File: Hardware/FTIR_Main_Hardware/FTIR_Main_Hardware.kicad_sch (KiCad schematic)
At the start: 63 parts, among them J1 RJ45_LED_Shielded, Q1 IRF7606PBF, Q2 BSS138, Q3 IRF7606PBF, Q4 IRF7606PBF, Q5 BSS138, Q6 BSS138, U1 Opamp_Dual, U2 D36V28F7, U3 OKI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

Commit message: Laser Diode Footprint
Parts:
- LD1: footprint (none) -> MRDT_Actives:DIO_PL_450B
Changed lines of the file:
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@@
       (effects (font (size 1.27 1.27)) (justify left))
     )
-    (property "Footprint" "" (at 205.105 171.45 0)
+    (property "Footprint" "MRDT_Actives:DIO_PL_450B" (at 205.105 171.45 0)
       (effects (font (size 1.27 1.27)) hide)
     )

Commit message: Footprints for LD and Stepper Driver fr this time
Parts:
- LD1: footprint MRDT_Actives:DIO_PL_450B -> Pakcage:DIO_PL_450B
- U1: footprint Package_SO:SO-8_3.9x4.9mm_P1.27mm -> (none)
- U2: footprint MRDT_Devices:D36V28F7_Buck -> (none)
- U4: footprint MRDT_Shields:MODULE_TMC2208_SILENTSTEPSTICK -> Pakcage:MODULE_TMC2208_SILENTSTEPSTICK
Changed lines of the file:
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@@
       (effects (font (size 1.27 1.27)))
     )
-    (property "Footprint" "Package_SO:SO-8_3.9x4.9mm_P1.27mm" (at 40.005 180.975 0)
+    (property "Footprint" "" (at 40.005 180.975 0)
       (effects (font (size 1.27 1.27)) hide)
     )
@@
       (effects (font (size 1.27 1.27)))
     )
-    (property "Footprint" "MRDT_Devices:D36V28F7_Buck" (at 40.64 75.565 0)
+    (property "Footprint" "" (at 40.64 75.565 0)
       (effects (font (size 1.27 1.27)) hide)
     )
@@
       (effects (font (size 1.27 1.27)))
     )
-    (property "Footprint" "MRDT_Shields:MODULE_TMC2208_SILENTSTEPSTICK" (at 87.63 115.57 0)
+    (property "Footprint" "Pakcage:MODULE_TMC2208_SILENTSTEPSTICK" (at 87.63 115.57 0)
       (effects (font (size 1.27 1.27)) hide)
     )
@@
       (effects (font (size 1.27 1.27)))
     )
-    (property "Footprint" "Package_SO:SO-8_3.9x4.9mm_P1.27mm" (at 102.235 181.61 0)
+    (property "Footprint" "" (at 102.235 181.61 0)
       (effects (font (size 1.27 1.27)) hide)
     )
@@
       (effects (font (size 1.27 1.27)))
     )
-    (property "Footprint" "Package_SO:SO-8_3.9x4.9mm_P1.27mm" (at 72.39 153.67 0)
+    (property "Footprint" "" (at 72.39 153.67 0)
       (effects (font (size 1.27 1.27)) hide)
     )
@@
       (effects (font (size 1.27 1.27)) (justify left))
     )
-    (property "Footprint" "MRDT_Actives:DIO_PL_450B" (at 205.105 171.45 0)
-      (effects (font (size 1.27 1.27)) hide)
-    )
+    (property "Footprint" "Pakcage:DIO_PL_450B" (at 205.105 171.45 0)
+      (effects (font (size 1.27 1.27)) hide)
+    )

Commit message: Fixed footprints??????
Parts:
- LD1: footprint Pakcage:DIO_PL_450B -> FTIR_Footprints:DIO_PL_450B
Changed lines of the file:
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@@
       (effects (font (size 1.27 1.27)) (justify left))
     )
-    (property "Footprint" "Pakcage:DIO_PL_450B" (at 205.105 171.45 0)
+    (property "Footprint" "FTIR_Footprints:DIO_PL_450B" (at 205.105 171.45 0)
       (effects (font (size 1.27 1.27)) hide)
     )

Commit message: Checked Footprints
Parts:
- U4: footprint Pakcage:MODULE_TMC2208_SILENTSTEPSTICK -> FTIR_Footprints:MODULE_TMC2208_SILENTSTEPSTICK
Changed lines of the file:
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@@
       (effects (font (size 1.27 1.27)))
     )
-    (property "Footprint" "Pakcage:MODULE_TMC2208_SILENTSTEPSTICK" (at 87.63 115.57 0)
+    (property "Footprint" "FTIR_Footprints:MODULE_TMC2208_SILENTSTEPSTICK" (at 87.63 115.57 0)
       (effects (font (size 1.27 1.27)) hide)
     )

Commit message: Finished Footprints (!)
I want to sleep :(
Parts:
- Conn10, Conn3, Conn5, Conn9: footprint (none) -> MRDT_Connectors:142-0701-801
- D1: footprint (none) -> MRDT_Sensors:P16113-011MN
- D3: footprint (none) -> MRDT_Sensors:VTP9812FH
- LD1: footprint FTIR_Footprints:DIO_PL_450B -> FTIR_Footprints:RLD63NPC5
- U1: footprint (none) -> Package_SO:SO-8_3.9x4.9mm_P1.27mm
- U2: footprint (none) -> MRDT_Devices:D36V28F7_Buck
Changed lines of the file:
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@@
       (effects (font (size 1.27 1.27)))
     )
-    (property "Footprint" "" (at 40.005 180.975 0)
+    (property "Footprint" "Package_SO:SO-8_3.9x4.9mm_P1.27mm" (at 40.005 180.975 0)
       (effects (font (size 1.27 1.27)) hide)
     )
@@
       (effects (font (size 1.27 1.27)))
     )
-    (property "Footprint" "" (at 40.64 75.565 0)
+    (property "Footprint" "MRDT_Devices:D36V28F7_Buck" (at 40.64 75.565 0)
       (effects (font (size 1.27 1.27)) hide)
     )
@@
       (effects (font (size 1.27 1.27)))
     )
-    (property "Footprint" "" (at 102.235 181.61 0)
+    (property "Footprint" "Package_SO:SO-8_3.9x4.9mm_P1.27mm" (at 102.235 181.61 0)
       (effects (font (size 1.27 1.27)) hide)
     )
@@
       (effects (font (size 1.27 1.27)) (justify left))
     )
-    (property "Footprint" "" (at 86.995 184.785 0)
+    (property "Footprint" "MRDT_Sensors:VTP9812FH" (at 86.995 184.785 0)
       (effects (font (size 1.27 1.27)) hide)
     )
@@
       (effects (font (size 1.27 1.27)))
     )
-    (property "Footprint" "" (at 72.39 153.67 0)
+    (property "Footprint" "Package_SO:SO-8_3.9x4.9mm_P1.27mm" (at 72.39 153.67 0)
       (effects (font (size 1.27 1.27)) hide)
     )
@@
       (effects (font (size 1.27 1.27)) (justify left))
     )
-    (property "Footprint" "FTIR_Footprints:DIO_PL_450B" (at 205.105 171.45 0)
+    (property "Footprint" "FTIR_Footprints:RLD63NPC5" (at 205.105 171.45 0)
       (effects (font (size 1.27 1.27)) hide)
     )
@@
       (effects (font (size 1.524 1.524)) (justify right))
     )
-    (property "Footprint" "" (at 65.405 180.975 0)
+    (property "Footprint" "MRDT_Connectors:142-0701-801" (at 65.405 180.975 0)
       (effects (font (size 1.524 1.524)) hide)
     )
@@
       (effects (font (size 1.27 1.27)) (justify left))
     )
-    (property "Footprint" "" (at 24.765 184.15 0)
+    (property "Footprint" "MRDT_Sensors:P16113-011MN" (at 24.765 184.15 0)
       (effects (font (size 1.27 1.27)) hide)
     )
@@
       (effects (font (size 1.524 1.524)) (justify right))
     )
-    (property "Footprint" "" (at 126.365 181.61 0)
+    (property "Footprint" "MRDT_Connectors:142-0701-801" (at 126.365 181.61 0)
       (effects (font (size 1.524 1.524)) hide)
     )
@@
       (effects (font (size 1.524 1.524)) (justify right))
     )
-    (property "Footprint" "" (at 202.565 112.395 0)
+    (property "Footprint" "MRDT_Connectors:142-0701-801" (at 202.565 112.395 0)
       (effects (font (size 1.524 1.524)) hide)
     )
@@
       (effects (font (size 1.524 1.524)) (justify right))
     )
-    (property "Footprint" "" (at 266.065 112.395 0)
-      (effects (font (size 1.524 1.524)) hide)
-    )
+    (property "Footprint" "MRDT_Connectors:142-0701-801" (at 266.065 112.395 0)
+      (effects (font (size 1.524 1.524)) hide)
+    )

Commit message: Moved footprints to local folder
Should work now?
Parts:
- Conn10, Conn3, Conn5, Conn9: footprint MRDT_Connectors:142-0701-801 -> FTIR_Footprints:142-0701-801
- D1: footprint MRDT_Sensors:P16113-011MN -> FTIR_Footprints:P16113-011MN
- D3: footprint MRDT_Sensors:VTP9812FH -> FTIR_Footprints:VTP9812FH
- U2: footprint MRDT_Devices:D36V28F7_Buck -> FTIR_Footprints:D36V28F7_Buck
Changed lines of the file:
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@@
       (effects (font (size 1.27 1.27)))
     )
-    (property "Footprint" "MRDT_Devices:D36V28F7_Buck" (at 40.64 75.565 0)
+    (property "Footprint" "FTIR_Footprints:D36V28F7_Buck" (at 40.64 75.565 0)
       (effects (font (size 1.27 1.27)) hide)
     )
@@
       (effects (font (size 1.27 1.27)) (justify left))
     )
-    (property "Footprint" "MRDT_Sensors:VTP9812FH" (at 86.995 184.785 0)
+    (property "Footprint" "FTIR_Footprints:VTP9812FH" (at 86.995 184.785 0)
       (effects (font (size 1.27 1.27)) hide)
     )
@@
       (effects (font (size 1.524 1.524)) (justify right))
     )
-    (property "Footprint" "MRDT_Connectors:142-0701-801" (at 65.405 180.975 0)
+    (property "Footprint" "FTIR_Footprints:142-0701-801" (at 65.405 180.975 0)
       (effects (font (size 1.524 1.524)) hide)
     )
@@
       (effects (font (size 1.27 1.27)) (justify left))
     )
-    (property "Footprint" "MRDT_Sensors:P16113-011MN" (at 24.765 184.15 0)
+    (property "Footprint" "FTIR_Footprints:P16113-011MN" (at 24.765 184.15 0)
       (effects (font (size 1.27 1.27)) hide)
     )
@@
       (effects (font (size 1.524 1.524)) (justify right))
     )
-    (property "Footprint" "MRDT_Connectors:142-0701-801" (at 126.365 181.61 0)
+    (property "Footprint" "FTIR_Footprints:142-0701-801" (at 126.365 181.61 0)
       (effects (font (size 1.524 1.524)) hide)
     )
@@
       (effects (font (size 1.524 1.524)) (justify right))
     )
-    (property "Footprint" "MRDT_Connectors:142-0701-801" (at 202.565 112.395 0)
+    (property "Footprint" "FTIR_Footprints:142-0701-801" (at 202.565 112.395 0)
       (effects (font (size 1.524 1.524)) hide)
     )
@@
       (effects (font (size 1.524 1.524)) (justify right))
     )
-    (property "Footprint" "MRDT_Connectors:142-0701-801" (at 266.065 112.395 0)
-      (effects (font (size 1.524 1.524)) hide)
-    )
+    (property "Footprint" "FTIR_Footprints:142-0701-801" (at 266.065 112.395 0)
+      (effects (font (size 1.524 1.524)) hide)
+    )

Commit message: Began Layout
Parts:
- removed D1: D_Photo, FTIR_Footprints:P16113-011MN, symbol Device:D_Photo
- removed D3: D_Photo, FTIR_Footprints:VTP9812FH, symbol Device:D_Photo
- added D1: D_Photo, FTIR_Footprints:VTP9812FH, symbol Sensor_Optical:S5971
- added D11: S5971, FTIR_Footprints:P16113-011MN, symbol Sensor_Optical:S5971
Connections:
- net GND: now also D1.3 (A), D11.3 (A)
- net at R1.1, U1.2 (-): now also D11.1 (K)
- net at R5.1, U1.6 (-): now also D1.1 (K)

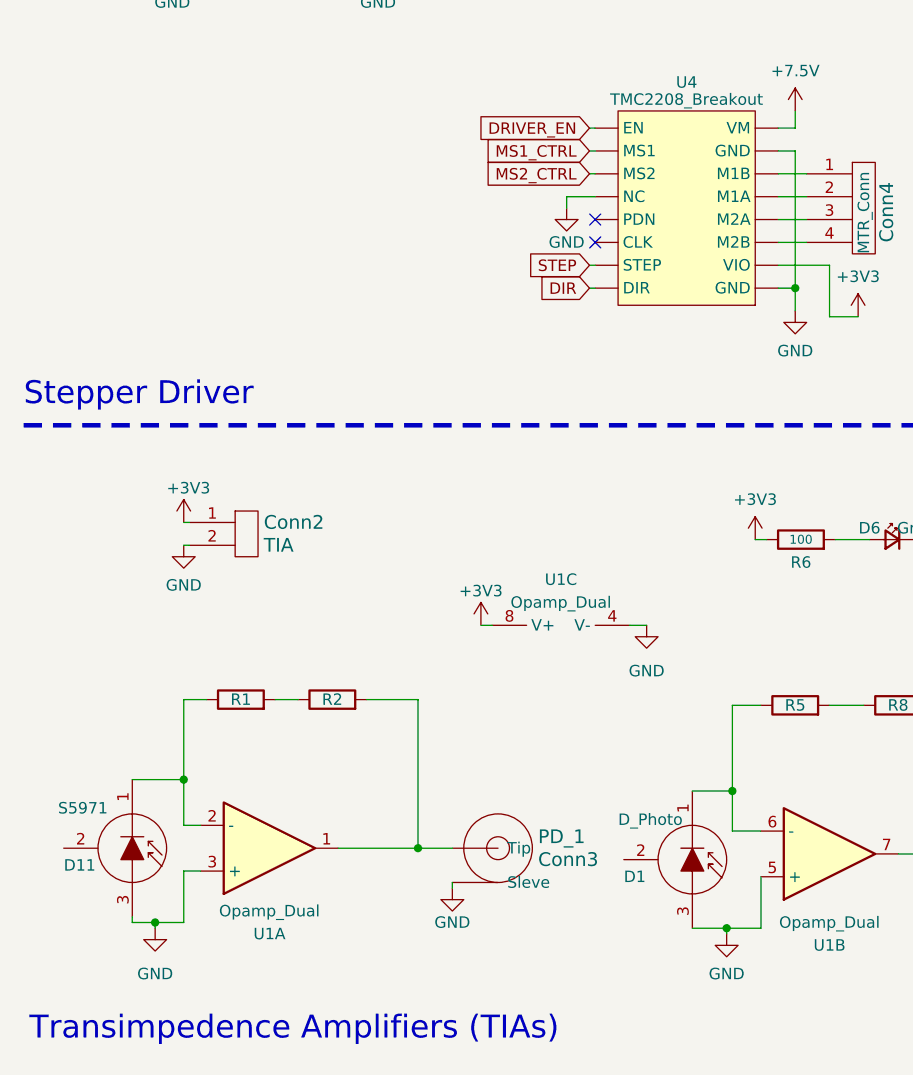
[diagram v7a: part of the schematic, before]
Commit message: updating footprint libraries
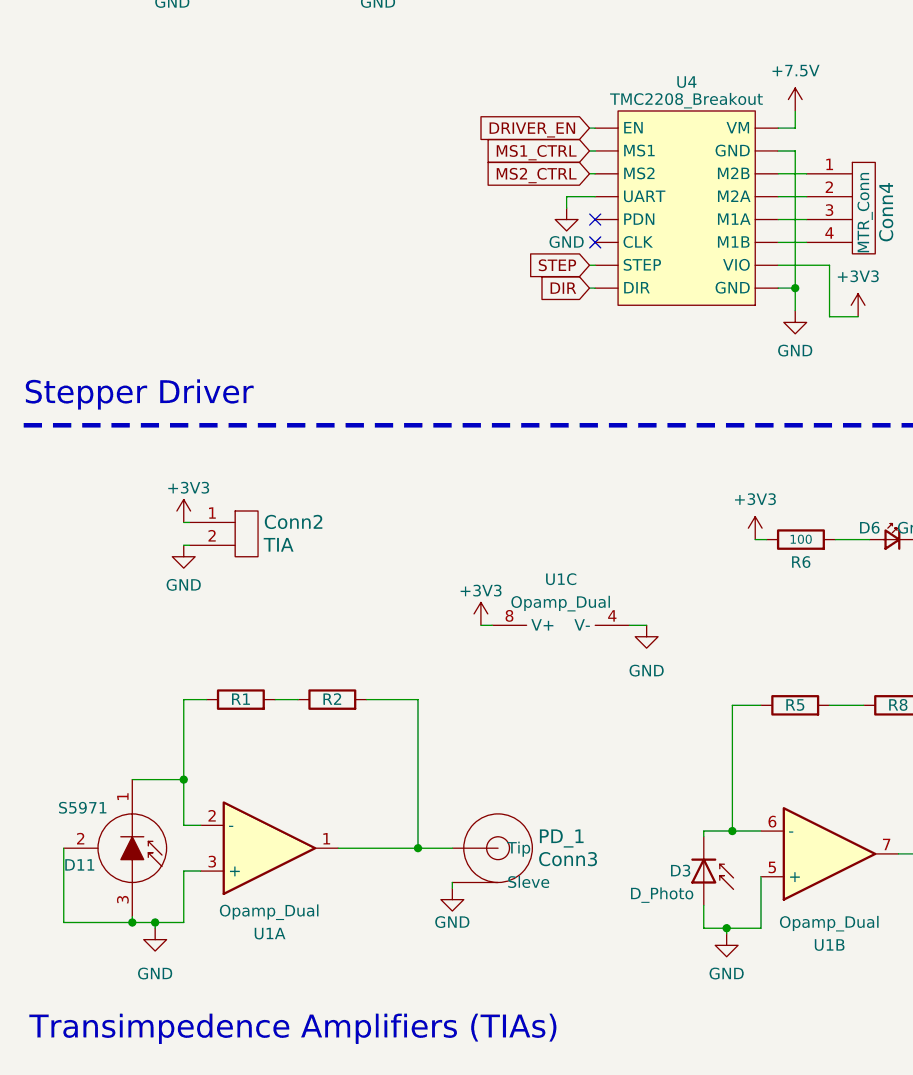
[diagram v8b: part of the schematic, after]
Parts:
- removed D1: D_Photo, FTIR_Footprints:VTP9812FH, symbol Sensor_Optical:S5971
- added D3: D_Photo, FTIR_Footprints:VTP9812FH, symbol Device:D_Photo
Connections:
- net GND: now also D11.2 (C), D3.2 (A)
- net at R5.1, U1.6 (-): now also D3.1 (K)
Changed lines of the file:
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@@
     (company "Mars Rover Design Team")
   )
-  (junction (at 90.805 189.865) (diameter 0) (color 0 0 0 0)
-  )
   (junction (at 305.435 26.67) (diameter 0) (color 0 0 0 0)
   )
@@
   (junction (at 156.845 117.475) (diameter 0) (color 0 0 0 0)
   )
+  (junction (at 91.44 179.07) (diameter 0) (color 0 0 0 0)
+  )
   (junction (at 27.305 189.23) (diameter 0) (color 0 0 0 0)
   )
   (junction (at 30.48 173.355) (diameter 0) (color 0 0 0 0)
   )
-  (junction (at 91.44 174.625) (diameter 0) (color 0 0 0 0)
-  )
   (junction (at 45.72 38.735) (diameter 0) (color 0 0 0 0)
   )
@@
   (junction (at 297.18 38.1) (diameter 0) (color 0 0 0 0)
   )
+  (junction (at 90.805 189.865) (diameter 0) (color 0 0 0 0)
+  )
   (junction (at 117.475 181.61) (diameter 0) (color 0 0 0 0)
   )
@@
   (junction (at 133.985 52.705) (diameter 0) (color 0 0 0 0)
   )
+  (junction (at 24.765 189.23) (diameter 0) (color 0 0 0 0)
+  )
   (junction (at 98.425 118.745) (diameter 0) (color 0 0 0 0)
   )
@@
     (stroke (width 0) (type default))
   )
+  (wire (pts (xy 91.44 179.07) (xy 94.615 179.07))
+    (stroke (width 0) (type default))
+  )
   (wire (pts (xy 56.515 180.975) (xy 60.325 180.975))
     (stroke (width 0) (type default))
@@
     (stroke (width 0) (type default))
   )
-  (wire (pts (xy 91.44 174.625) (xy 91.44 179.07))
-    (stroke (width 0) (type default))
-  )
   (wire (pts (xy 90.805 189.865) (xy 94.615 189.865))
     (stroke (width 0) (type default))
@@
     (stroke (width 0) (type default))
   )
-  (wire (pts (xy 86.995 189.865) (xy 90.805 189.865))
-    (stroke (width 0) (type default))
-  )
   (wire (pts (xy 300.355 113.03) (xy 300.355 111.76))
     (stroke (width 0) (type default))
@@
     (stroke (width 0) (type default))
   )
+  (wire (pts (xy 91.44 165.1) (xy 91.44 179.07))
+    (stroke (width 0) (type default))
+  )
   (wire (pts (xy 297.18 38.1) (xy 300.355 38.1))
     (stroke (width 0) (type default))
@@
     (stroke (width 0.508) (type dash_dot_dot))
   )
+  (wire (pts (xy 88.265 179.705) (xy 88.265 179.07))
+    (stroke (width 0) (type default))
+  )
   (wire (pts (xy 69.85 28.575) (xy 73.66 28.575))
     (stroke (width 0) (type default))
@@
     (stroke (width 0) (type dash))
   )
-  (wire (pts (xy 91.44 179.07) (xy 94.615 179.07))
+  (wire (pts (xy 88.265 179.07) (xy 91.44 179.07))
     (stroke (width 0) (type default))
   )
@@
     (stroke (width 0) (type default))
   )
-  (wire (pts (xy 91.44 165.1) (xy 91.44 174.625))
-    (stroke (width 0) (type default))
-  )
   (wire (pts (xy 178.435 154.305) (xy 180.34 154.305))
     (stroke (width 0) (type default))
@@
     (stroke (width 0) (type default))
   )
-  (wire (pts (xy 86.995 174.625) (xy 91.44 174.625))
-    (stroke (width 0) (type default))
-  )
   (wire (pts (xy 154.305 45.085) (xy 154.305 44.45))
     (stroke (width 0) (type default))
@@
     (stroke (width 0) (type default))
   )
+  (wire (pts (xy 17.145 189.23) (xy 24.765 189.23))
+    (stroke (width 0) (type default))
+  )
   (polyline (pts (xy 343.535 102.87) (xy 287.655 102.87))
     (stroke (width 0) (type dash))
@@
     (stroke (width 0) (type default))
   )
+  (wire (pts (xy 88.265 187.325) (xy 88.265 189.865))
+    (stroke (width 0) (type default))
+  )
   (wire (pts (xy 41.91 38.735) (xy 45.72 38.735))
     (stroke (width 0) (type default))
   )
+  (wire (pts (xy 17.145 180.975) (xy 17.145 189.23))
+    (stroke (width 0) (type default))
+  )
   (wire (pts (xy 81.915 156.21) (xy 80.01 156.21))
     (stroke (width 0) (type default))
@@
     (stroke (width 0) (type default))
   )
+  (wire (pts (xy 88.265 189.865) (xy 90.805 189.865))
+    (stroke (width 0) (type default))
+  )
   (wire (pts (xy 260.35 116.205) (xy 260.985 116.205))
     (stroke (width 0) (type default))
@@
     )
   )
-  (symbol (lib_id "Sensor_Optical:S5971") (at 86.995 182.245 270) (unit 1)
-    (in_bom yes) (on_board yes) (dnp no)
-    (property "Reference" "D1" (at 79.375 184.15 90)
-      (effects (font (size 1.27 1.27)) (justify left))
-    )
-    (property "Value" "D_Photo" (at 78.74 177.8 90)
-      (effects (font (size 1.27 1.27)) (justify left))
-    )
-    (property "Footprint" "FTIR_Footprints:VTP9812FH" (at 95.885 182.245 0)
-      (effects (font (size 1.27 1.27)) hide)
-    )
-    (property "Datasheet" "https://www.digikey.com/en/products/detail/excelitas-technologies/VTP9812FH/5885875" (at 86.995 182.245 0)
-      (effects (font (size 1.27 1.27)) hide)
-    )
-    (pin "2")
-    (pin "1")
-    (pin "3")
-    (instances
-      (project "FTIR_Main_Hardware"
-        (path "/049c3f09-c046-40c3-9872-e62b40667976"
-          (reference "D1") (unit 1)
-        )
-      )
-    )
-  )
   (symbol (lib_id "Device:R") (at 98.425 165.1 90) (unit 1)
     (in_bom yes) (on_board yes) (dnp no)
@@
         )
       )
+    )
+  )
+  (symbol (lib_id "Device:D_Photo") (at 88.265 184.785 270) (unit 1)
+    (in_bom yes) (on_board yes) (dnp no)
+    (property "Reference" "D3" (at 84.455 183.515 90)
+      (effects (font (size 1.27 1.27)) (justify left))
+    )
+    (property "Value" "D_Photo" (at 80.01 186.055 90)
+      (effects (font (size 1.27 1.27)) (justify left))
+    )
+    (property "Footprint" "FTIR_Footprints:VTP9812FH" (at 88.265 183.515 0)
+      (effects (font (size 1.27 1.27)) hide)
+    )
+    (property "Datasheet" "https://www.digikey.com/en/products/detail/excelitas-technologies/VTP9812FH/5885875" (at 88.265 183.515 0)
+      (effects (font (size 1.27 1.27)) hide)
+    )
+    (pin "1")
+    (pin "2")
+    (instances
+      (project "FTIR_Main_Hardware"
+        (path "/049c3f09-c046-40c3-9872-e62b40667976"
+          (reference "D3") (unit 1)
+        )
+      )
